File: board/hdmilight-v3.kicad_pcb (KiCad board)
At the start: 2 copper layers, 100 x 100 mm, 254 parts, among them J1 USB_B_Micro, J10 Conn_01x08, J11 Screw_Terminal_01x02, J12 Conn_01x02_Male, J13 Conn_01x16_Male, J2 HDMI_A, J3 Conn_01x02_Male, J4 Conn_01x08, J5 Conn_01x08, J6 Conn_01x08, J7 Conn_02x05_Odd_Even, J8 6P6C, J9 6P6C, Q1 FDD6530A, Q2 BSS123, Q3 BSS123, Q4 BSS123, SW1 SW_Push, SW2 SW_Push, U1 STM32F303RETx, U10 74HC245, U11 74HC245, U12 TPS65266, U2 93CxxB, U3 FT2232D, U4 ADV7611, U5 XC6SLX9-TQG144, U6 TPD12S520, U7 AT25SF081-SSHD-X, U8 74HC245, U9 74HC245, X1 SG-310SCF-32MHz, Y1 6MHz, Y2 28.6363MHz

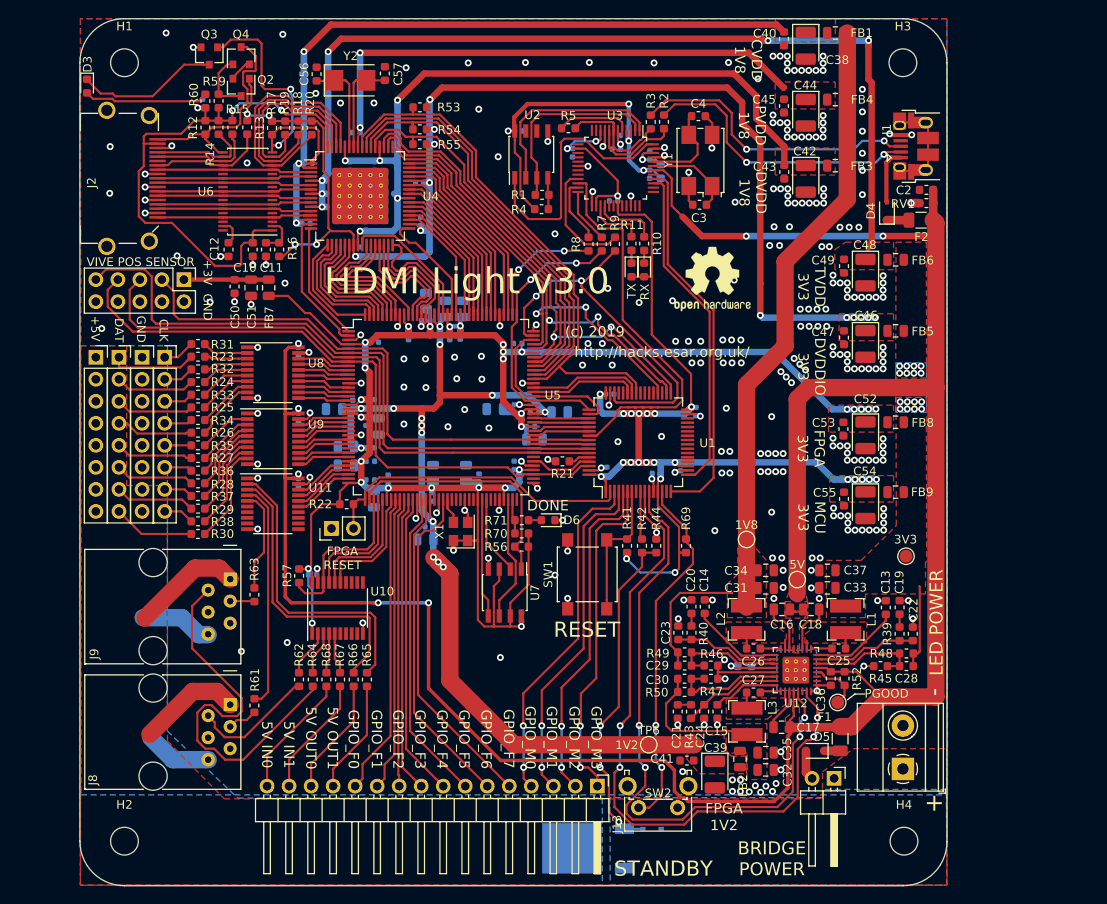
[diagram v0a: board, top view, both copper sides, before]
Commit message: Fixed bugs in v3.0 board:
 * Changed FPGA GPIO to 2 row with ground to make it compatible with logic analyser plug for debugging
 * Move position sensor from PB4 to PB5
 * Connect voltage regulator center pad to ground pins
 * Add SPI CS line between FPGA and MCU
 * Move HDMI hotplug LED back from board edge
 * Move HDMI ESD chip closer to connector
 * Swap serial rx/tx
 * Fix FPGA EEPROM footprint
 * Fix reset button footprint
 * Connect ADV I2C to MCU
 * Fix missing ground to hotplug power off circuit
 * Move LED power connector to back of board
 * Move standby button to front of board
 * Only use HDMI 5v for hotplug detect
 * Change LED power switching to high side to stop it grounding back through the data line
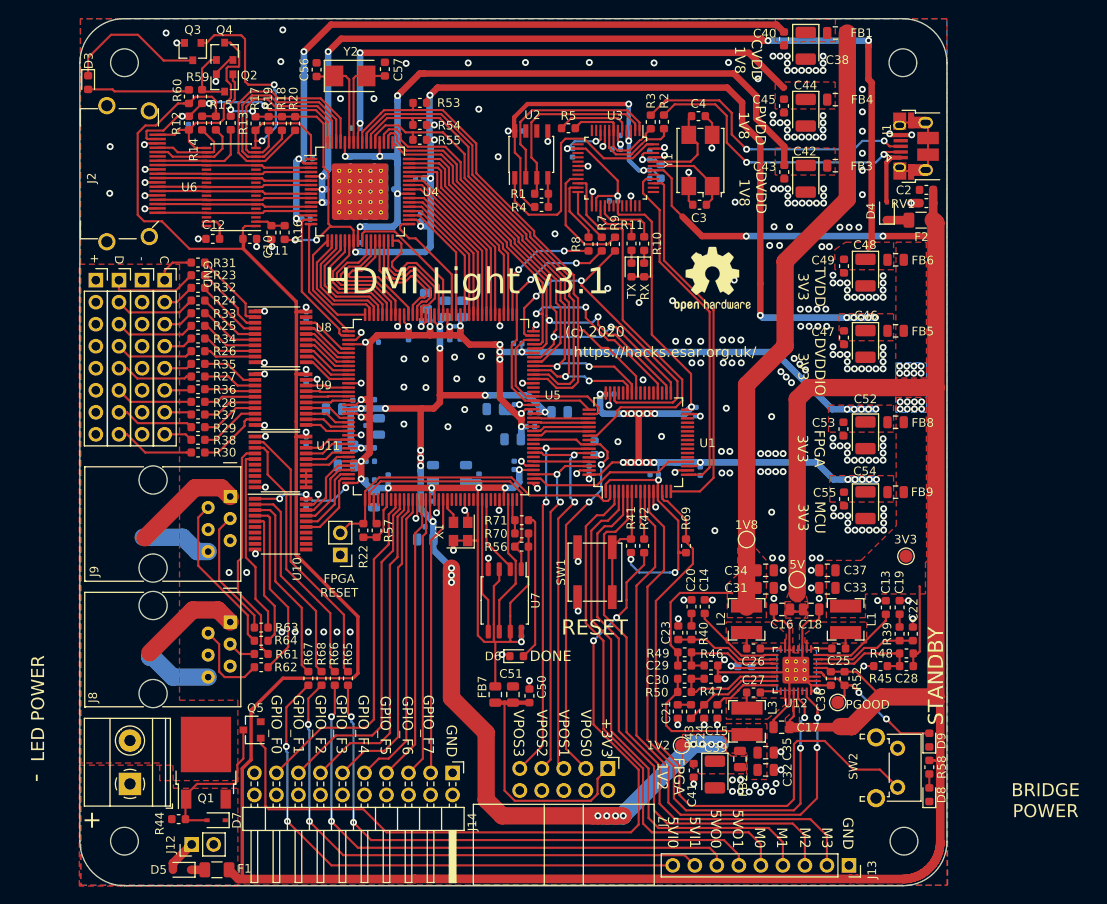
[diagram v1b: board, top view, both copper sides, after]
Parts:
- added D8: LED, LED_SMD:LED_0603_1608Metric, F.Cu at (173.0, 129.5)
- added D9: LED, LED_SMD:LED_0603_1608Metric, F.Cu at (173.0, 123.2)
- added J14: Conn_02x10_Odd_Even, Connector_PinHeader_2.54mm:PinHeader_2x10_P2.54mm_Horizontal, F.Cu at (118.0, 127.0)
- added Q5: BSS123, Package_TO_SOT_SMD:SOT-23, F.Cu at (94.9, 122.0)
- added R58: 2K2, Resistor_SMD:R_0603_1608Metric, F.Cu at (173.0, 126.3)
- C3, C4: value 27pF -> 12pF
- D7: moved to F.Cu
- J12: footprint Connector_PinHeader_2.54mm:PinHeader_1x02_P2.54mm_Horizontal -> Connector_PinHeader_2.54mm:PinHeader_1x02_P2.54mm_Vertical
- J13: value Conn_01x16_Male -> Conn_01x09; footprint Connector_PinHeader_2.54mm:PinHeader_1x16_P2.54mm_Horizontal -> Connector_PinSocket_2.54mm:PinSocket_1x09_P2.54mm_Vertical
- J7: footprint Connector_PinHeader_2.54mm:PinHeader_2x05_P2.54mm_Vertical -> Connector_IDC:IDC-Header_2x05_P2.54mm_Horizontal
- Q1: value FDD6530A -> SUD50P04-08; moved to F.Cu
- R21: moved to B.Cu
- R52: value 10K -> 2K2
- R60: value 1K -> 2K2
- SW1: footprint Button_Switch_SMD:SW_SPST_B3S-1000 -> Button_Switch_SMD:SW_SPST_EVQP0
- U10, U11, U8, U9: value 74HC245 -> 74LV245
- U7: value AT25SF081-SSHD-X -> S25FL064L; footprint Package_SO:SOIC-8_3.9x4.9mm_P1.27mm -> Package_SO:SOIC-8_5.23x5.23mm_P1.27mm
- Y2: value 28.6363MHz -> 28.63636MHz
- moved J11 89.2 mm to (80.8, 128.3)
- moved J7 74.6 mm to (135.9, 126.5)
- moved J12 74.5 mm to (87.9, 135.3), turned to 90 degrees
- moved D5 74.3 mm to (86.8, 138.2)
- moved F1 73.5 mm to (90.8, 138.2), turned to 180 degrees
- moved R44 63.5 mm to (86.4, 132.3), turned to 0 degrees
- moved C50 58.2 mm to (126.8, 118.1), turned to 90 degrees
- moved C51 55.8 mm to (124.9, 118.0), turned to 90 degrees
- moved FB7 53.7 mm to (122.9, 118.0), turned to 90 degrees
- moved D7 50.3 mm to (90.7, 132.5), turned to 180 degrees
- moved Q1 45.2 mm to (89.5, 125.8), turned to 90 degrees
- moved J13 30.4 mm to (163.7, 137.7)
- moved SW2 26.3 mm to (169.3, 124.2), turned to 270 degrees
- moved D6 16.1 mm to (125.4, 113.5), turned to 0 degrees
- moved U10 11.7 mm to (98.1, 98.3), turned to 0 degrees
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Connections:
- C10 pad 1: HDMI_5V -> +5V
- D7 pad 2: GND -> Net-(D7-Pad2)
- J11 pad 1: /hdmilight-v3-io/LED_POWER -> Net-(D7-Pad1)
- J12 pad 1: /hdmilight-v3-io/LED_POWER -> Net-(D5-Pad2)
- J12 pad 2: Net-(D5-Pad2) -> Net-(D7-Pad1)
- J13 pad 1: /hdmilight-v3-io/MCU_GPIO3 -> GND
- J13 pad 2: /hdmilight-v3-io/MCU_GPIO2 -> /hdmilight-v3-io/MCU_GPIO3
- J13 pad 3: /hdmilight-v3-io/MCU_GPIO1 -> /hdmilight-v3-io/MCU_GPIO2
- J13 pad 4: /hdmilight-v3-microcontroller/MCU_GPIO0 -> /hdmilight-v3-io/MCU_GPIO1
- J13 pad 5: /hdmilight-v3-fpga/FPGA_GPIO7 -> /hdmilight-v3-microcontroller/MCU_GPIO0
- J13 pad 6: /hdmilight-v3-fpga/FPGA_GPIO6 -> Net-(J13-Pad6)
- J13 pad 7: /hdmilight-v3-fpga/FPGA_GPIO5 -> Net-(J13-Pad7)
- J13 pad 8: /hdmilight-v3-fpga/FPGA_GPIO4 -> Net-(J13-Pad8)
- J13 pad 9: /hdmilight-v3-fpga/FPGA_GPIO3 -> Net-(J13-Pad9)
- J6 pad 1: /hdmilight-v3-io/LED_GND -> GND
- J6 pad 2: /hdmilight-v3-io/LED_GND -> GND
- J6 pad 3: /hdmilight-v3-io/LED_GND -> GND
- J6 pad 4: /hdmilight-v3-io/LED_GND -> GND
- J6 pad 5: /hdmilight-v3-io/LED_GND -> GND
- J6 pad 6: /hdmilight-v3-io/LED_GND -> GND
- J6 pad 7: /hdmilight-v3-io/LED_GND -> GND
- J6 pad 8: /hdmilight-v3-io/LED_GND -> GND
- J8 pad 6: /hdmilight-v3-io/LED_GND -> GND
- J9 pad 6: /hdmilight-v3-io/LED_GND -> GND
- Q1 pad 1: Net-(D7-Pad1) -> Net-(D7-Pad2)
- Q1 pad 2: /hdmilight-v3-io/LED_GND -> /hdmilight-v3-io/LED_POWER
- Q1 pad 3: GND -> Net-(D7-Pad1)
- Q2 pad 2: Net-(Q2-Pad2) -> GND
- Q4 pad 2: Net-(Q2-Pad2) -> GND
- R14 pad 1: HDMI_5V -> +5V
- R15 pad 1: HDMI_5V -> +5V
- R42 pad 2: Net-(D7-Pad1) -> Net-(Q5-Pad1)
- R44 pad 1: GND -> Net-(D7-Pad1)
- R44 pad 2: Net-(D7-Pad1) -> Net-(D7-Pad2)
- R57 pad 2: /hdmilight-v3-fpga/PAPIX_POS0 -> Net-(R57-Pad2)
- R60 pad 2: HDMI_5V -> +5V
- R65 pad 2: Net-(J13-Pad13) -> Net-(J13-Pad6)
- R66 pad 2: Net-(J13-Pad14) -> Net-(J13-Pad7)
- R67 pad 1: /hdmilight-v3-io/5V_INPUT_CON1 -> /hdmilight-v3-io/5V_INPUT_CON0
- R67 pad 2: Net-(J13-Pad15) -> Net-(J13-Pad9)
- R68 pad 1: /hdmilight-v3-io/5V_INPUT_CON0 -> /hdmilight-v3-io/5V_INPUT_CON1
- R68 pad 2: Net-(J13-Pad16) -> Net-(J13-Pad8)
- U1 pad 20: Net-(U1-Pad20) -> /hdmilight-v3-fpga/SPI_NSS
- U1 pad 42: /hdmilight-v3-microcontroller/I2C_SCL -> /hdmilight-v3-fpga/ADV_SCL
- U1 pad 43: /hdmilight-v3-microcontroller/I2C_SDA -> /hdmilight-v3-fpga/ADV_SDA
- U1 pad 56: /hdmilight-v3-fpga/POS_SENSOR0 -> /hdmilight-v3-microcontroller/JRST
- U1 pad 57: /hdmilight-v3-fpga/MCU_PB5 -> /hdmilight-v3-fpga/POS_SENSOR0
- U10 pad 15: /hdmilight-v3-fpga/5V_INPUT1 -> /hdmilight-v3-fpga/PAPIX_POS1
- U10 pad 16: /hdmilight-v3-fpga/5V_INPUT0 -> /hdmilight-v3-fpga/PAPIX_POS0
- U10 pad 17: /hdmilight-v3-fpga/PAPIX_POS1 -> /hdmilight-v3-fpga/5V_INPUT0
- U10 pad 18: /hdmilight-v3-fpga/PAPIX_POS0 -> /hdmilight-v3-fpga/5V_INPUT1
- U10 pad 2: Net-(R62-Pad1) -> /hdmilight-v3-io/5V_INPUT_CON1
- U10 pad 3: Net-(R64-Pad1) -> /hdmilight-v3-io/5V_INPUT_CON0
- U10 pad 4: /hdmilight-v3-io/5V_INPUT_CON0 -> Net-(R62-Pad1)
- U10 pad 5: /hdmilight-v3-io/5V_INPUT_CON1 -> Net-(R64-Pad1)
- U3 pad 39: /hdmilight-v3-microcontroller/RXD -> /hdmilight-v3-microcontroller/TXD
- U3 pad 40: /hdmilight-v3-microcontroller/TXD -> /hdmilight-v3-microcontroller/RXD
- U5 pad 10: /hdmilight-v3-fpga/LED_OUT1 -> /hdmilight-v3-fpga/LED_OUT5
- U5 pad 11: /hdmilight-v3-fpga/LED_OUT2 -> /hdmilight-v3-fpga/LED_OUT6
- U5 pad 12: /hdmilight-v3-fpga/LED_OUT3 -> /hdmilight-v3-fpga/LED_OUT7
- U5 pad 14: /hdmilight-v3-fpga/LED_OUT4 -> /hdmilight-v3-fpga/LED_OUT8
- U5 pad 15: /hdmilight-v3-fpga/LED_OUT5 -> /hdmilight-v3-fpga/LED_OUT9
- U5 pad 16: /hdmilight-v3-fpga/LED_OUT6 -> /hdmilight-v3-fpga/LED_OUT10
- U5 pad 17: /hdmilight-v3-fpga/LED_OUT7 -> /hdmilight-v3-fpga/LED_OUT11
- U5 pad 21: /hdmilight-v3-fpga/LED_OUT8 -> /hdmilight-v3-fpga/LED_OUT12
- U5 pad 22: /hdmilight-v3-fpga/LED_OUT9 -> /hdmilight-v3-fpga/LED_OUT13
- U5 pad 23: /hdmilight-v3-fpga/LED_OUT10 -> /hdmilight-v3-fpga/LED_OUT14
- U5 pad 24: /hdmilight-v3-fpga/LED_OUT11 -> /hdmilight-v3-fpga/LED_OUT15
- U5 pad 26: /hdmilight-v3-fpga/LED_OUT12 -> /hdmilight-v3-fpga/5V_OUTPUT0
- U5 pad 27: /hdmilight-v3-fpga/LED_OUT13 -> /hdmilight-v3-fpga/5V_OUTPUT1
- U5 pad 29: /hdmilight-v3-fpga/LED_OUT14 -> /hdmilight-v3-fpga/PAPIX_RGB0
- U5 pad 30: /hdmilight-v3-fpga/LED_OUT15 -> /hdmilight-v3-fpga/PAPIX_RGB1
- U5 pad 32: /hdmilight-v3-fpga/5V_OUTPUT0 -> /hdmilight-v3-fpga/5V_INPUT1
- U5 pad 33: /hdmilight-v3-fpga/5V_OUTPUT1 -> /hdmilight-v3-fpga/5V_INPUT0
- U5 pad 34: /hdmilight-v3-fpga/PAPIX_RGB0 -> /hdmilight-v3-fpga/PAPIX_POS0
- U5 pad 35: /hdmilight-v3-fpga/PAPIX_RGB1 -> /hdmilight-v3-fpga/PAPIX_POS1
- U5 pad 39: /hdmilight-v3-fpga/PAPIX_POS0 -> Net-(R57-Pad2)
- U5 pad 40: /hdmilight-v3-fpga/PAPIX_POS1 -> Net-(U5-Pad40)
- U5 pad 41: /hdmilight-v3-fpga/5V_INPUT0 -> Net-(U5-Pad41)
- U5 pad 43: /hdmilight-v3-fpga/5V_INPUT1 -> Net-(U5-Pad43)
- U5 pad 5: /hdmilight-v3-fpga/POS_SENSOR0 -> /hdmilight-v3-fpga/LED_OUT0
- U5 pad 6: /hdmilight-v3-fpga/POS_SENSOR3 -> /hdmilight-v3-fpga/LED_OUT1
- U5 pad 7: /hdmilight-v3-fpga/POS_SENSOR1 -> /hdmilight-v3-fpga/LED_OUT2
- U5 pad 74: Net-(U5-Pad74) -> /hdmilight-v3-fpga/SPI_NSS
- U5 pad 8: /hdmilight-v3-fpga/POS_SENSOR2 -> /hdmilight-v3-fpga/LED_OUT3
- U5 pad 82: /hdmilight-v3-fpga/MCU_PB5 -> Net-(U5-Pad82)
- U5 pad 9: /hdmilight-v3-fpga/LED_OUT0 -> /hdmilight-v3-fpga/LED_OUT4
- U5 pad 94: /hdmilight-v3-microcontroller/I2C_SDA -> Net-(U5-Pad94)
- U5 pad 95: /hdmilight-v3-microcontroller/I2C_SCL -> Net-(U5-Pad95)
- U6 pad 1: HDMI_5V -> +5V
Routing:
- net +5V: track 330.5 -> 451.6 mm, vias 11 -> 9
- net Net-(Q5-Pad1): track 0.00 -> 88.7 mm, vias 0 -> 2
- net Net-(J13-Pad9): track 0.00 -> 63.4 mm, vias 0 -> 2
- net Net-(J13-Pad6): track 0.00 -> 63.3 mm, vias 0 -> 2
- net Net-(J13-Pad7): track 0.00 -> 63.1 mm, vias 0 -> 2
- net Net-(J13-Pad8): track 0.00 -> 62.9 mm, vias 0 -> 2
- net Net-(D7-Pad1): track 38.8 -> 0.00 mm, vias 3 -> 0
- net HDMI_5V: track 63.8 -> 28.4 mm
- net Net-(R69-Pad2): track 41.9 -> 74.3 mm, vias 2 -> 0
- net /hdmilight-v3-fpga/POS_SENSOR2: track 73.9 -> 42.1 mm, vias 0 -> 2
- net /hdmilight-v3-fpga/POS_SENSOR3: track 74.9 -> 44.7 mm, vias 0 -> 2
- net /hdmilight-v3-fpga/POS_SENSOR1: track 70.4 -> 44.2 mm, vias 0 -> 2
- net Net-(J9-Pad2): track 44.6 -> 18.5 mm
- net /hdmilight-v3-io/MCU_GPIO3: track 39.0 -> 64.7 mm, vias 2 -> 0
- net /hdmilight-v3-io/MCU_GPIO2: track 38.9 -> 63.2 mm, vias 2 -> 0
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- added copper zone on F.Cu, net Net-(D7-Pad1)
- removed copper zone on B.Cu, net /hdmilight-v3-io/LED_GND
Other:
- board text added: "(c) 2020"
- board text added: "+3V3"
- board text added: "5VI0"
- board text added: "5VI1"
- board text added: "5VO0"
- board text added: "5VO1"
- board text added: "C"
- board text added: "D"
- board text added: "HDMI Light v3.1"
- board text added: "M0"
- board text added: "M1"
- board text added: "M2"
- board text added: "M3"
- board text added: "VPOS0"
- board text added: "VPOS1"
- board text added: "VPOS2"
- board text added: "VPOS3"
- board text added: "https://hacks.esar.org.uk/"
- board text removed: "(c) 2019"
- board text removed: "+3V"
- board text removed: "+5V"
- board text removed: "5V IN0"
- board text removed: "5V IN1"
- board text removed: "5V OUT0"
- board text removed: "5V OUT1"
- board text removed: "CLK"
- board text removed: "DAT"
- board text removed: "GPIO_M0"
- board text removed: "GPIO_M1"
- board text removed: "GPIO_M2"
- board text removed: "GPIO_M3"
- board text removed: "HDMI Light v3.0"
- board text removed: "VIVE POS SENSOR"
- board text removed: "http://hacks.esar.org.uk/"

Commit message: removed old unused silscreen labels
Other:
- board text removed: "BRIDGE POWER"
- board text removed: "LED POWER"
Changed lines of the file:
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@@
   (general
     (thickness 1.6)
-    (drawings 62)
+    (drawings 59)
     (tracks 3005)
     (zones 0)
@@
     (effects (font (size 3 3) (thickness 0.5)))
   )
-  (gr_text - (at 69.85 127.5715 90) (layer F.SilkS)
-    (effects (font (size 2 2) (thickness 0.4)))
-  )
   (gr_text + (at 76.327 132.461 90) (layer F.SilkS)
     (effects (font (size 2 2) (thickness 0.4)))
   )
-  (gr_text "LED POWER" (at 70.1675 119.5705 90) (layer F.SilkS)
-    (effects (font (size 1.5 1.5) (thickness 0.3)))
-  )
-  (gr_text "BRIDGE\nPOWER" (at 186.3852 130.2004) (layer F.SilkS)
-    (effects (font (size 1.5 1.5) (thickness 0.3)))
-  )
   (gr_text RESET (at 134.366 110.236) (layer F.SilkS)

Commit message: Updated BOM with individual LED colours/types
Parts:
- D1, D6: value LED -> LED Red
- D2: value LED -> LED Green
- D3, D8: value LED -> LED Side Red
- D9: value LED -> LED Side Green
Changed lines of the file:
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@@
       (effects (font (size 1 1) (thickness 0.15)))
     )
-    (fp_text value LED (at 0 1.43 90) (layer F.Fab)
+    (fp_text value "LED Side Green" (at 0 1.43 90) (layer F.Fab)
       (effects (font (size 1 1) (thickness 0.15)))
     )
@@
       (effects (font (size 1 1) (thickness 0.15)))
     )
-    (fp_text value LED (at 0 1.43 90) (layer F.Fab)
+    (fp_text value "LED Side Red" (at 0 1.43 90) (layer F.Fab)
       (effects (font (size 1 1) (thickness 0.15)))
     )
@@
       (effects (font (size 1 1) (thickness 0.15)))
     )
-    (fp_text value LED (at 0 1.43) (layer F.Fab)
+    (fp_text value "LED Red" (at 0 1.43) (layer F.Fab)
       (effects (font (size 1 1) (thickness 0.15)))
     )
@@
       (effects (font (size 1 1) (thickness 0.15)))
     )
-    (fp_text value LED (at 0 1.43 90) (layer F.Fab)
+    (fp_text value "LED Side Red" (at 0 1.43 90) (layer F.Fab)
       (effects (font (size 1 1) (thickness 0.15)))
     )
@@
       (effects (font (size 1 1) (thickness 0.15)))
     )
-    (fp_text value LED (at 0 1.43 270) (layer F.Fab)
+    (fp_text value "LED Red" (at 0 1.43 270) (layer F.Fab)
       (effects (font (size 1 1) (thickness 0.15)))
     )
@@
       (effects (font (size 1 1) (thickness 0.15)))
     )
-    (fp_text value LED (at 0 1.43 270) (layer F.Fab)
+    (fp_text value "LED Green" (at 0 1.43 270) (layer F.Fab)
       (effects (font (size 1 1) (thickness 0.15)))
     )
